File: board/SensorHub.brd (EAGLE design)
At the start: 99.1 x 68.2 mm, 36 parts, among them IC1 PIC12F629P, X1 RJ45-6LC21-B, X2 RJ45-6LC21-B, X3 RJ45-6LC21-B, X4 RJ45-6LC21-B, X5 RJ45-6LC21-B, X6 RJ45-6LC21-B, X7 RJ45-6LC21-B, X8 RJ45-6LC21-B, X9 22-23-2081

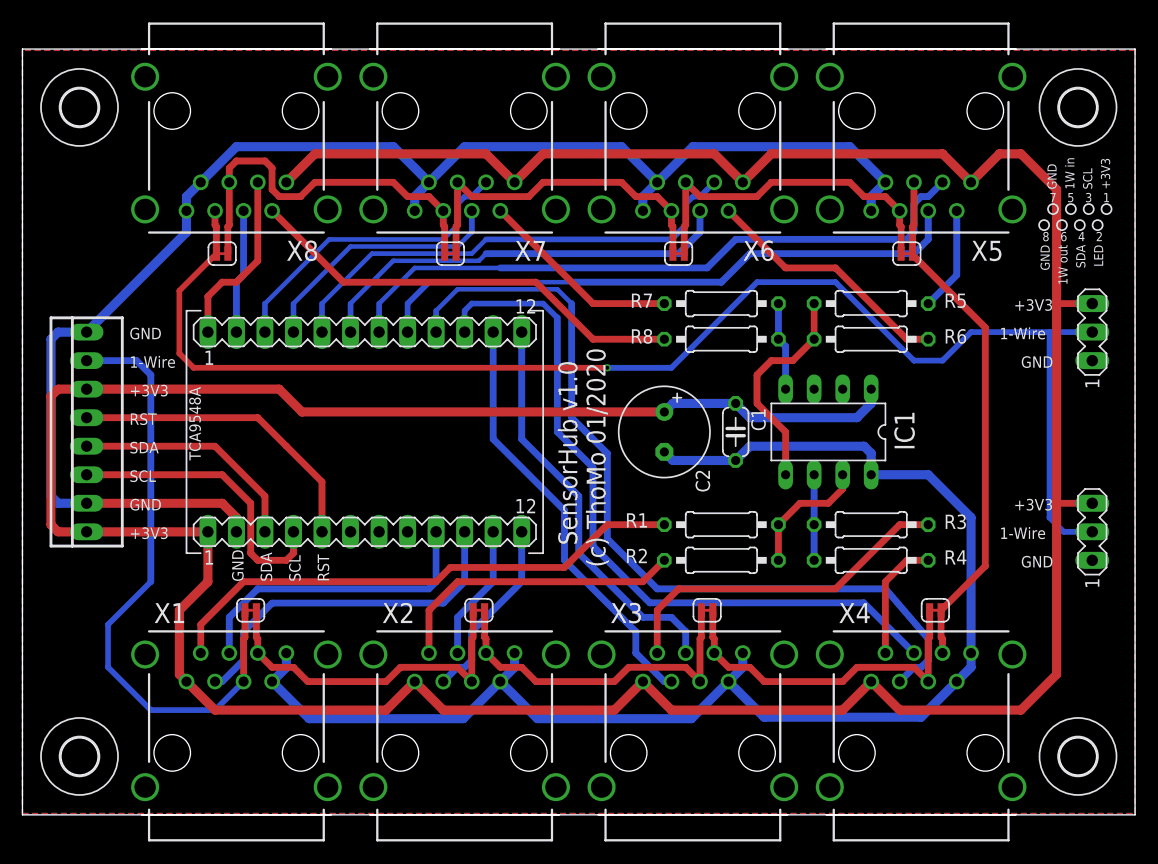
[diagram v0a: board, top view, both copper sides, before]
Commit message: sensor hub with power lines only
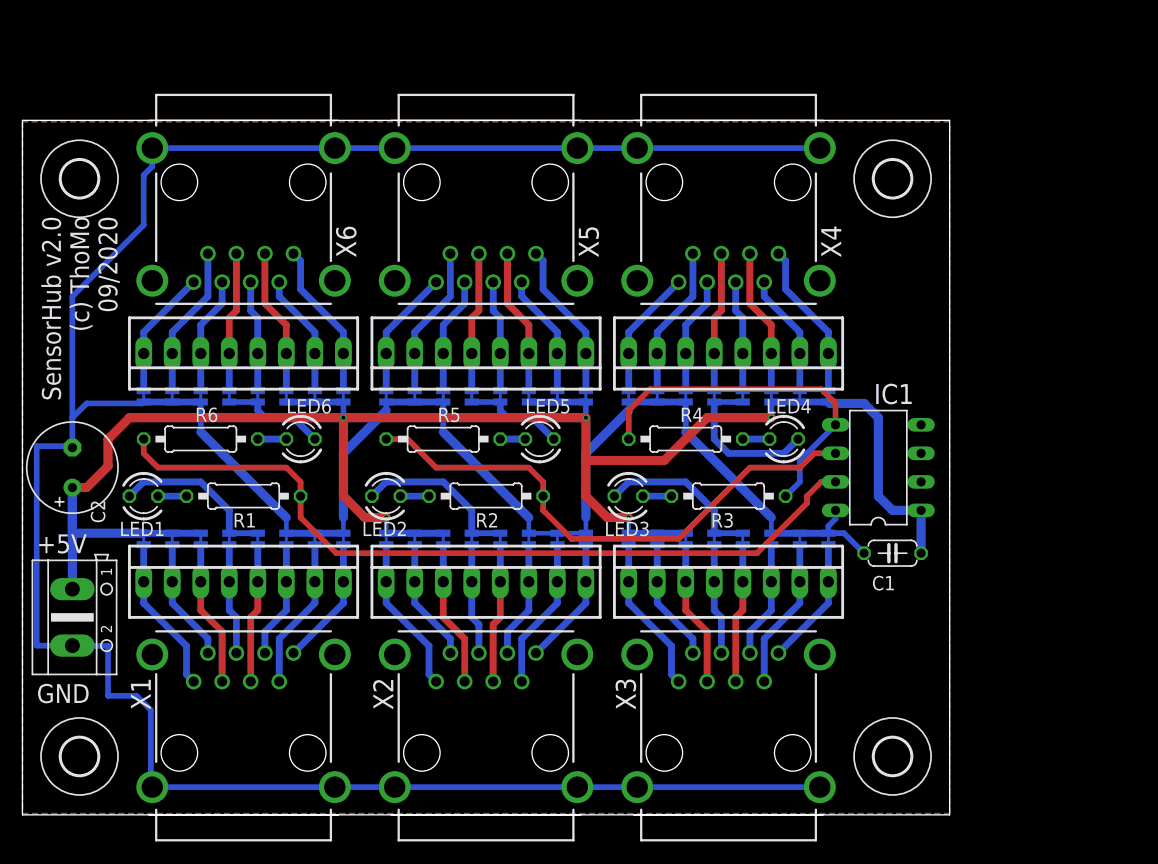
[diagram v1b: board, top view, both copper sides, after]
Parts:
- removed R7, R8: (no value), rcl:0207/10
- removed SJ1, SJ2, SJ3, SJ4, SJ5, SJ6, SJ7, SJ8: JUMPER-SMT_2_NC_TRACE_SILK, SparkFun-Jumpers:SMT-JUMPER_2_NC_TRACE_SILK
- removed SV1, SV2: (no value), con-lstb:MA12-1
- removed SV3, SV4: (no value), con-lstb:MA03-1
- removed X7: RJ45-6LC21-B, con-tycoelectronics:RJ45-SHIELD1
- removed X9: 22-23-2081, con-molex:22-23-2081
- added JP1, JP10, JP11, JP12, JP13, JP14, JP15, JP16, JP17, JP18, JP19, JP2, JP20, JP21, JP22, JP23, JP24, JP25, JP26, JP27, JP28, JP29, JP3, JP30, JP31, JP32, JP33, JP34, JP35, JP36, JP37, JP38, JP39, JP4, JP40, JP41, JP42, JP43, JP44, JP45, JP46, JP47, JP48, JP5, JP6, JP7, JP8, JP9: JUMPER-SMT_2_NC_TRACE_SILK, SparkFun-Jumpers:SMT-JUMPER_2_NC_TRACE_SILK
- added LED1, LED2, LED3, LED4, LED5, LED6: TLLR4400, led:LED3MM
- added X1.1, X1.2, X1.3, X1.4, X1.5, X1.6: 22-23-2081, con-molex:22-23-2081
- X8: value RJ45-6LC21-B -> (none); device con-tycoelectronics:RJ45-SHIELD1 -> con-ptr500:AK500/2
- moved R6 60.3 mm to (15.9, 34.3)
- moved X4 53.6 mm to (62.9, 57.1), turned to 180 degrees
- moved C2 52.8 mm to (4.45, 31.8), turned to 90 degrees
- moved X8 47.4 mm to (4.45, 18.4), turned to 270 degrees
- moved R1 42.6 mm to (19.7, 29.2)
- moved X6 40.5 mm to (19.7, 57.1)
- moved R5 40.0 mm to (37.5, 34.3)
- moved X5 39.3 mm to (41.3, 57.1)
- moved R2 21.7 mm to (41.3, 29.2)
- moved R4 19.7 mm to (59.1, 34.3)
- moved U$3 17.7 mm to (77.5, 57.5)
- moved C1 17.7 mm to (77.5, 24.1), turned to 180 degrees
- moved U$4 16.5 mm to (77.5, 6.03)
- moved R3 13.0 mm to (62.9, 29.2), turned to 180 degrees
- moved U$2 6.35 mm to (5.08, 57.5)
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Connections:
- removed net +3V3: C1.1, C2.+, IC1.1, SV1.1, SV3.3, SV4.3, X1.1, X2.1, X3.1, X4.1, X5.1, X6.1, X7.1, X8.1, X9.1, X9.6
- removed net LED0: R1.2, X1.2
- removed net LED7: R8.1, X8.2
- removed net ONEWIRE: SJ1.2, X1.5, X9.7
- removed net OW_OUT: SJ8.1, SV3.2, SV4.2, X8.6
- removed net RST: SV1.5, X9.5
- removed net SC0: SV1.10, X1.3
- removed net SC1: SV1.12, X2.3
- removed net SC2: SV2.11, X3.3
- removed net SC3: SV2.9, X4.3
- removed net SC4: SV2.7, X5.3
- removed net SC5: SV2.5, X6.3
- removed net SC6: SV2.3, X7.3
- removed net SC7: SV2.1, X8.3
- removed net SCL: SV1.4, X9.3
- removed net SD0: SV1.9, X1.4
- removed net SD1: SV1.11, X2.4
- removed net SD2: SV2.12, X3.4
- removed net SD3: SV2.10, X4.4
- removed net SD4: SV2.8, X5.4
- removed net SD5: SV2.6, X6.4
- removed net SD6: SV2.4, X7.4
- removed net SD7: SV2.2, X8.4
- removed net SDA: SV1.3, X9.4
- new net +5V: C1.1, C2.+, IC1.1, JP1.2, JP10.2, JP11.2, JP17.2, JP18.2, JP19.2, JP2.2, JP25.2, JP26.2, JP27.2, JP3.2, JP33.2, JP34.2, JP35.2, JP41.2, JP42.2, JP43.2, JP9.2, X8.1
- new net N$1: JP1.1, X1.1, X1.1.1
- new net N$11: LED1.K, R1.2
- new net N$13: LED3.K, R3.2
- new net N$15: LED5.K, R5.2
- new net N$16: LED4.K, R4.2
- new net N$17: JP10.1, X1.2.2, X2.2
- new net N$19: JP12.1, X1.2.4, X2.4
- new net N$2: JP2.1, X1.1.2, X1.2
- new net N$23: JP14.1, X1.2.6, X2.6
- new net N$24: JP15.1, X1.2.7, X2.7
- new net N$25: JP16.1, X1.2.8, X2.8
- new net N$26: JP17.1, X1.3.1, X3.1
- new net N$27: JP18.1, X1.3.2, X3.2
- new net N$28: JP19.1, X1.3.3, X3.3
- new net N$29: JP20.1, X1.3.4, X3.4
- new net N$30: JP21.1, X1.3.5, X3.5
- new net N$31: JP22.1, X1.3.6, X3.6
- new net N$32: JP23.1, X1.3.7, X3.7
- new net N$33: JP24.1, X1.3.8, X3.8
- new net N$34: JP25.1, X1.4.1, X4.1
- new net N$35: JP26.1, X1.4.2, X4.2
- new net N$36: JP27.1, X1.4.3, X4.3
- new net N$37: JP28.1, X1.4.4, X4.4
- new net N$38: JP29.1, X1.4.5, X4.5
- new net N$39: JP30.1, X1.4.6, X4.6
- new net N$4: JP4.1, X1.1.4, X1.4
- new net N$40: JP31.1, X1.4.7, X4.7
- new net N$41: JP32.1, X1.4.8, X4.8
- new net N$42: JP33.1, X1.5.1, X5.1
- new net N$43: JP34.1, X1.5.2, X5.2
- new net N$44: JP35.1, X1.5.3, X5.3
- new net N$45: JP36.1, X1.5.4, X5.4
- new net N$46: JP37.1, X1.5.5, X5.5
- new net N$47: JP38.1, X1.5.6, X5.6
- new net N$48: JP39.1, X1.5.7, X5.7
- new net N$49: JP40.1, X1.5.8, X5.8
- new net N$50: JP41.1, X1.6.1, X6.1
- new net N$51: JP42.1, X1.6.2, X6.2
- new net N$52: JP43.1, X1.6.3, X6.3
- new net N$53: JP44.1, X1.6.4, X6.4
- new net N$54: JP45.1, X1.6.5, X6.5
- new net N$55: JP46.1, X1.6.6, X6.6
- new net N$56: JP47.1, X1.6.7, X6.7
- new net N$57: JP48.1, X1.6.8, X6.8
- new net N$6: JP6.1, X1.1.6, X1.6
- new net N$9: JP9.1, X1.2.1, X2.1
- net GND: now also JP14.2, JP15.2, JP16.2, JP22.2, JP23.2, JP24.2, JP30.2, JP31.2, JP32.2, JP38.2, JP39.2, JP40.2, JP46.2, JP47.2, JP48.2, JP6.2, JP7.2, JP8.2, X8.2; no longer SV1.2, SV3.1, SV4.1, X1.7, X1.8, X2.7, X2.8, X3.7, X3.8, X4.7, X4.8, X5.7, X5.8, X6.7, X6.8, X7.7, X7.8, X7.S1, X7.S2, X8.7, X8.8, X8.S1, X8.S2, X9.2, X9.8
- net LED1: now also JP4.2, JP5.2, LED1.A; no longer R2.2, X2.2
- net LED2: now also JP12.2, JP13.2, LED2.A; no longer R3.2, X3.2
- net LED3: now also JP20.2, JP21.2, LED3.A; no longer R4.2, X4.2
- net LED4: now also JP28.2, JP29.2, LED4.A; no longer R5.2, X5.2
- net LED5: now also JP36.2, JP37.2, LED5.A; no longer R6.2, X6.2
- net LED6: now also JP44.2, JP45.2, LED6.A; no longer R7.1, X7.2
- net N$10: now also IC1.6, R2.1, R5.1; no longer SJ6.1, SJ7.2, X6.6, X7.5
- net N$12: now also LED2.K, R2.2; no longer SJ7.1, SJ8.2, X7.6, X8.5
- net N$14: now also LED6.K, R6.2; no longer SJ2.1, SJ3.2, X2.6, X3.5
- net N$18: now also JP11.1, X1.2.3, X2.3; no longer IC1.4, R7.2, R8.2
- net N$20: now also R6.1; no longer R2.1
- net N$21: now also JP13.1, X1.2.5, X2.5; no longer IC1.6, R3.1, R4.1
- net N$22: now also R3.1, R4.1; no longer R5.1, R6.1
- net N$3: now also JP3.1, X1.1.3, X1.3; no longer SJ3.1, SJ4.2, X3.6, X4.5
- net N$5: now also JP5.1, X1.1.5, X1.5; no longer SJ1.1, SJ2.2, X1.6, X2.5
- net N$7: now also JP7.1, X1.1.7, X1.7; no longer SJ4.1, SJ5.2, X4.6, X5.5
- net N$8: now also JP8.1, X1.1.8, X1.8; no longer SJ5.1, SJ6.2, X5.6, X6.5
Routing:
- net +3V3: track 330.0 -> 0.00 mm
- net +5V: track 0.00 -> 168.0 mm, vias 0 -> 5
- net OW_OUT: track 124.0 -> 0.00 mm, vias 1 -> 0
- net SC3: track 75.2 -> 0.00 mm
- net SD3: track 65.1 -> 0.00 mm
- net N$20: track 11.5 -> 71.4 mm
- net SC4: track 58.7 -> 0.00 mm
- net ONEWIRE: track 55.0 -> 0.00 mm
- net SD4: track 53.8 -> 0.00 mm
- net GND: track 256.9 -> 306.1 mm
- net LED0: track 47.5 -> 0.00 mm
- net SC5: track 43.1 -> 0.00 mm
- net LED7: track 39.7 -> 0.00 mm
- net SD5: track 38.2 -> 0.00 mm
- net SC2: track 38.1 -> 0.00 mm
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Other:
- board size 99.1 x 68.2 mm -> 82.5 x 61.8 mm
- board text added: "+5V"
- board text added: "SensorHub v2.0 (c) ThoMo 09/2020"
- board text removed: "+3V3"
- board text removed: "1"
- board text removed: "1-Wire"
- board text removed: "1W in"
- board text removed: "1W out"
- board text removed: "2"
- board text removed: "3"
- board text removed: "4"
- board text removed: "5"
- board text removed: "6"
- board text removed: "7"
- board text removed: "8"
- board text removed: "LED"
- board text removed: "RST"
- board text removed: "SCL"
- board text removed: "SDA"
- board text removed: "SensorHub v1.0 (c) ThoMo 01/2020"
- board text removed: "TCA9548A"
